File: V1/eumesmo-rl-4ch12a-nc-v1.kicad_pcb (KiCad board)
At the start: 2 copper layers, 68 x 67.8 mm, 25 parts, among them J1 250-202, J2 250-204, J3 DB142V-5.08-4P, J4 DB142V-5.08-4P, K1 Songle_SRD_1B, K2 Songle_SRD_1B, K3 Songle_SRD_1B, K4 Songle_SRD_1B

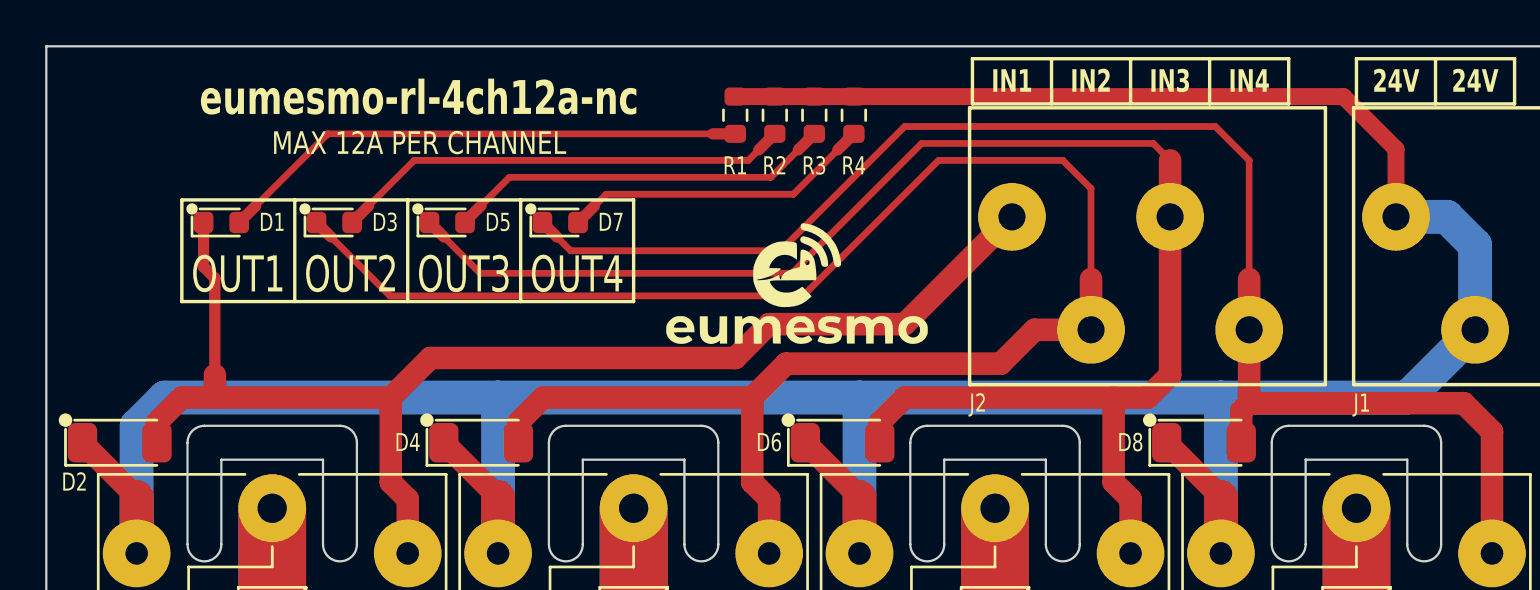
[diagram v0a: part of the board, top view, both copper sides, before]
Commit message: Replaced 0603 size 10k resistors for 0805 size.
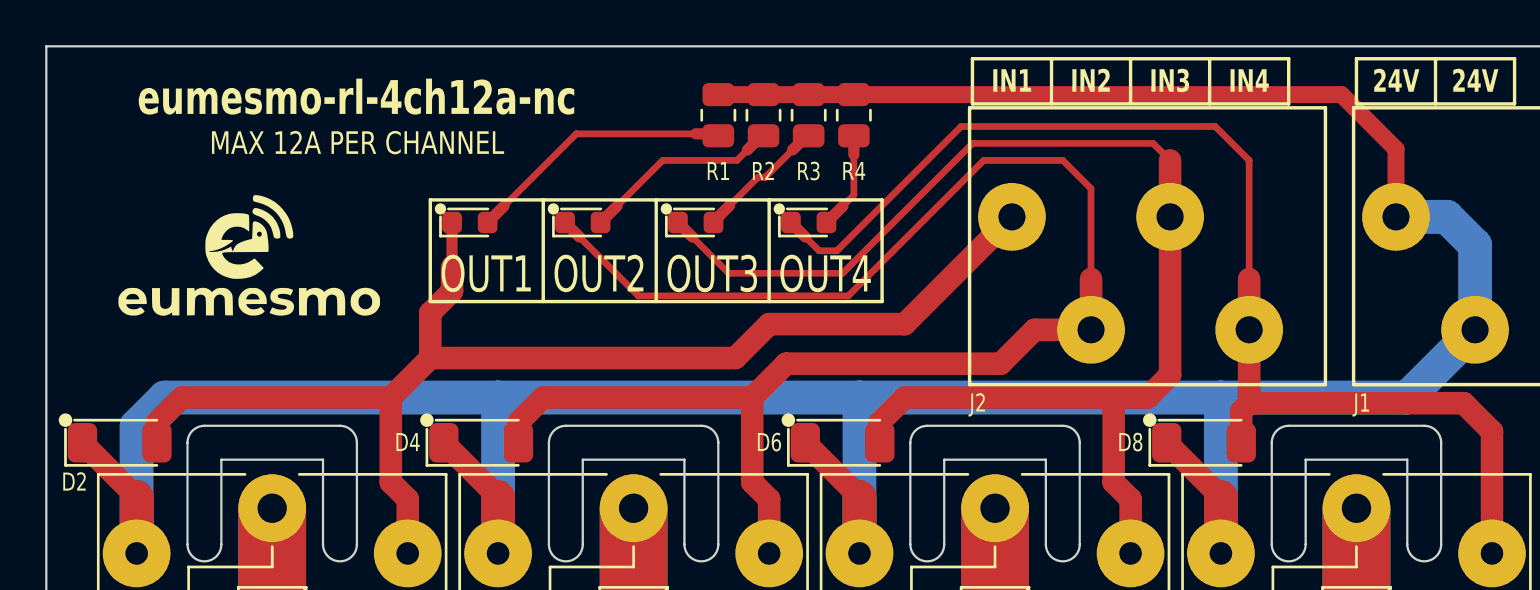
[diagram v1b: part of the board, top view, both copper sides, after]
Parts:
- R1, R2, R3, R4: value 10k/100mW -> 10k/125mW; footprint Tales:R_0603_1608Metric -> Tales:R_0805_2012Metric
- moved G*** 24.3 mm to (134.0, 71.5)
- moved D1 11.0 mm to (143.8, 70.0)
- moved D3 11.0 mm to (148.8, 70.0)
- moved D5 11.0 mm to (153.8, 70.0)
- moved D7 11.0 mm to (158.8, 70.0)
- moved R1 0.75 mm to (154.8, 65.2)
- moved R2 0.50 mm to (156.8, 65.2)
- moved R3 0.25 mm to (158.8, 65.2)
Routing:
- net /LED1: track 23.6 -> 11.8 mm
- net /LED2: track 20.3 -> 8.84 mm
- net /LED3: track 17.1 -> 5.86 mm
- net /IN4: track 64.0 -> 53.0 mm
- net /IN3: track 67.7 -> 56.7 mm
- net /IN2: track 80.0 -> 69.0 mm
- net /LED4: track 13.8 -> 4.34 mm
- net /IN1: track 57.7 -> 56.1 mm
- net +24V: track 151.9 -> 152.7 mm
